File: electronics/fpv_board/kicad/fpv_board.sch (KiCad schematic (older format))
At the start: 12 parts, among them K1 CONN_3, K2 CONN_3, K3 CONN_3, P1 CONN_2, P2 CONN_2, P3 CONN_1, SW1 SWITCH_INV, SW2 SWITCH_INV, SW3 4-SW_DIP, U1 LD1117DT33, U2 L78M05, U3 TX-5800-200

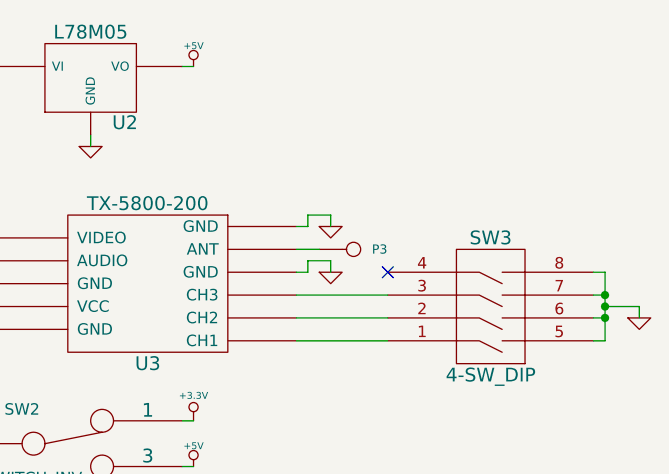
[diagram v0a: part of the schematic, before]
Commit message: Updated FPV board schematic. Started implementation of FPV board PCB. Added .gitignore
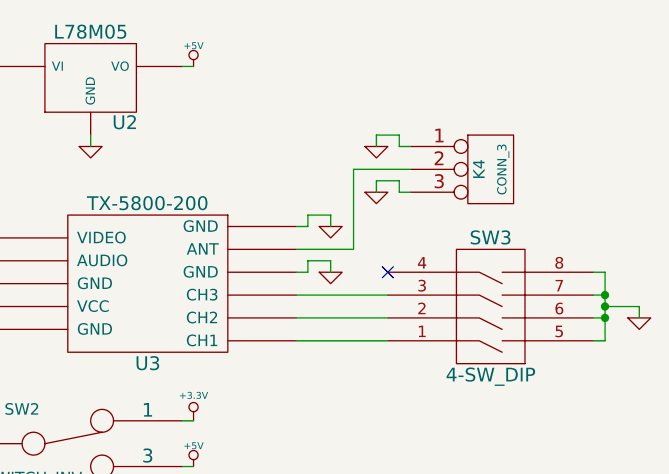
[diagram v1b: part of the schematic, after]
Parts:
- removed P3: CONN_1, symbol CONN_1
- added K4: CONN_3, symbol CONN_3
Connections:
- net GND: now also K4.1 (P1), K4.3 (P3)
- net at U3.10 (ANT): now also K4.2 (PM)
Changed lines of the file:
@@
 NoConn ~ 5350 2000
-$Comp
-L CONN_1 P3
-U 1 1 5381A5F5
-P 5200 1900
-F 0 "P3" H 5280 1900 40  0000 L CNN
-F 1 "CONN_1" H 5200 1955 30  0001 C CNN
-F 2 "" H 5200 1900 60  0000 C CNN
-F 3 "" H 5200 1900 60  0000 C CNN
-	1    5200 1900
-	1    0    0    -1
-$EndComp
-Wire Wire Line
-	4950 1900 5050 1900
 $Comp
 L SWITCH_INV SW1
@@
 	1    0    0    -1
 $EndComp
+$Comp
+L CONN_3 K4
+U 1 1 53826CEB
+P 5800 1550
+F 0 "K4" V 5750 1550 50  0000 C CNN
+F 1 "CONN_3" V 5850 1550 40  0000 C CNN
+F 2 "" H 5800 1550 60  0000 C CNN
+F 3 "" H 5800 1550 60  0000 C CNN
+	1    5800 1550
+	1    0    0    -1
+$EndComp
+$Comp
+L GND #PWR021
+U 1 1 53826CFA
+P 5300 1650
+F 0 "#PWR021" H 5300 1650 30  0001 C CNN
+F 1 "GND" H 5300 1580 30  0001 C CNN
+F 2 "" H 5300 1650 60  0000 C CNN
+F 3 "" H 5300 1650 60  0000 C CNN
+	1    5300 1650
+	1    0    0    -1
+$EndComp
+$Comp
+L GND #PWR022
+U 1 1 53826D09
+P 5300 1450
+F 0 "#PWR022" H 5300 1450 30  0001 C CNN
+F 1 "GND" H 5300 1380 30  0001 C CNN
+F 2 "" H 5300 1450 60  0000 C CNN
+F 3 "" H 5300 1450 60  0000 C CNN
+	1    5300 1450
+	1    0    0    -1
+$EndComp
+Wire Wire Line
+	5450 1450 5400 1450
+Wire Wire Line
+	5400 1450 5400 1400
+Wire Wire Line
+	5400 1400 5300 1400
+Wire Wire Line
+	5300 1400 5300 1450
+Wire Wire Line
+	5450 1650 5400 1650
+Wire Wire Line
+	5400 1650 5400 1600
+Wire Wire Line
+	5400 1600 5300 1600
+Wire Wire Line
+	5300 1600 5300 1650
+Wire Wire Line
+	5450 1550 5200 1550
+Wire Wire Line
+	5200 1550 5200 1900
+Wire Wire Line
+	5200 1900 4950 1900
 $EndSCHEMATC

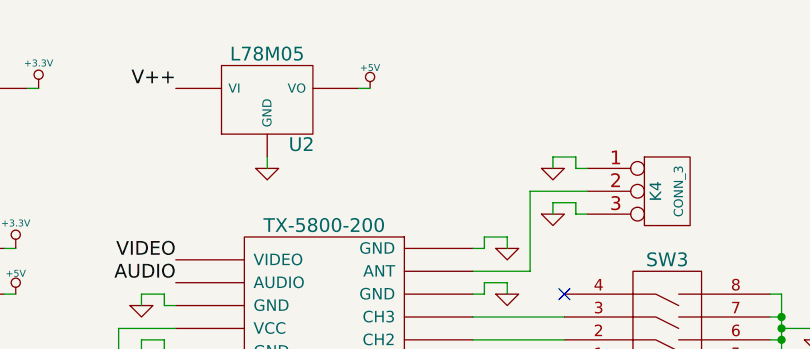
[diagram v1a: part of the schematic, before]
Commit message: Added 5V source selecter jumper to FPV board schematic. Implemented FPV PCB.
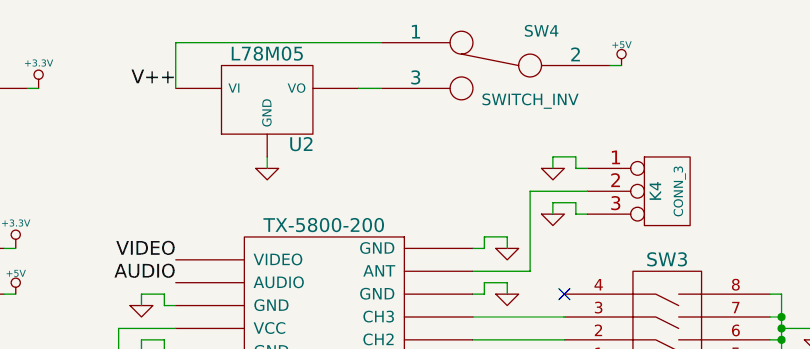
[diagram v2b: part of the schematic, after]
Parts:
- added SW4: SWITCH_INV, ~, symbol SWITCH_INV
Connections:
- net +5V: now also SW4.2; no longer U2.VO
- net V++: now also SW4.1
- new net: SW4.3, U2.VO
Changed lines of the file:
@@
 Sheet 1 1
 Title ""
-Date "25 may 2014"
+Date "27 may 2014"
 Rev ""
 Comp ""
@@
 V++
 $Comp
-L GND #PWR01
+L GND #PWR1
 U 1 1 53815D82
 P 1650 1400
-F 0 "#PWR01" H 1650 1400 30  0001 C CNN
+F 0 "#PWR1" H 1650 1400 30  0001 C CNN
 F 1 "GND" H 1650 1330 30  0001 C CNN
 F 2 "" H 1650 1400 60  0000 C CNN
@@
 $EndComp
 $Comp
-L GND #PWR02
+L GND #PWR2
 U 1 1 53816497
 P 1700 1800
-F 0 "#PWR02" H 1700 1800 30  0001 C CNN
+F 0 "#PWR2" H 1700 1800 30  0001 C CNN
 F 1 "GND" H 1700 1730 30  0001 C CNN
 F 2 "" H 1700 1800 60  0000 C CNN
@@
 $EndComp
 $Comp
-L GND #PWR03
+L GND #PWR4
 U 1 1 538183A2
 P 1700 2850
-F 0 "#PWR03" H 1700 2850 30  0001 C CNN
+F 0 "#PWR4" H 1700 2850 30  0001 C CNN
 F 1 "GND" H 1700 2780 30  0001 C CNN
 F 2 "" H 1700 2850 60  0000 C CNN
@@
 $EndComp
 $Comp
-L GND #PWR04
+L GND #PWR8
 U 1 1 538183B6
 P 2900 2850
-F 0 "#PWR04" H 2900 2850 30  0001 C CNN
+F 0 "#PWR8" H 2900 2850 30  0001 C CNN
 F 1 "GND" H 2900 2780 30  0001 C CNN
 F 2 "" H 2900 2850 60  0000 C CNN
@@
 	2900 2800 2900 2850
 $Comp
-L +5V #PWR05
+L +5V #PWR7
 U 1 1 538183E4
 P 2800 2700
-F 0 "#PWR05" H 2800 2790 20  0001 C CNN
+F 0 "#PWR7" H 2800 2790 20  0001 C CNN
 F 1 "+5V" H 2800 2790 30  0000 C CNN
 F 2 "" H 2800 2700 60  0000 C CNN
@@
 $EndComp
 $Comp
-L +5V #PWR06
+L +5V #PWR10
 U 1 1 538183F3
 P 2950 2000
-F 0 "#PWR06" H 2950 2090 20  0001 C CNN
+F 0 "#PWR10" H 2950 2090 20  0001 C CNN
 F 1 "+5V" H 2950 2090 30  0000 C CNN
 F 2 "" H 2950 2000 60  0000 C CNN
@@
 $EndComp
 $Comp
-L +3.3V #PWR07
+L +3.3V #PWR9
 U 1 1 53818406
 P 2950 1800
-F 0 "#PWR07" H 2950 1760 30  0001 C CNN
+F 0 "#PWR9" H 2950 1760 30  0001 C CNN
 F 1 "+3.3V" H 2950 1910 30  0000 C CNN
 F 2 "" H 2950 1800 60  0000 C CNN
@@
 $EndComp
 $Comp
-L +3.3V #PWR08
+L +3.3V #PWR6
 U 1 1 53818415
 P 2800 2600
-F 0 "#PWR08" H 2800 2560 30  0001 C CNN
+F 0 "#PWR6" H 2800 2560 30  0001 C CNN
 F 1 "+3.3V" H 2800 2710 30  0000 C CNN
 F 2 "" H 2800 2600 60  0000 C CNN
@@
 	2750 2600 2800 2600
 $Comp
-L GND #PWR09
+L GND #PWR3
 U 1 1 538184EF
 P 1700 2500
-F 0 "#PWR09" H 1700 2500 30  0001 C CNN
+F 0 "#PWR3" H 1700 2500 30  0001 C CNN
 F 1 "GND" H 1700 2430 30  0001 C CNN
 F 2 "" H 1700 2500 60  0000 C CNN
@@
 V++
 $Comp
-L +3.3V #PWR010
+L +3.3V #PWR11
 U 1 1 53818937
 P 3050 1100
-F 0 "#PWR010" H 3050 1060 30  0001 C CNN
+F 0 "#PWR11" H 3050 1060 30  0001 C CNN
 F 1 "+3.3V" H 3050 1210 30  0000 C CNN
 F 2 "" H 3050 1100 60  0000 C CNN
@@
 $EndComp
 $Comp
-L +5V #PWR011
+L +5V #PWR21
 U 1 1 53818946
-P 4500 1100
-F 0 "#PWR011" H 4500 1190 20  0001 C CNN
-F 1 "+5V" H 4500 1190 30  0000 C CNN
-F 2 "" H 4500 1100 60  0000 C CNN
-F 3 "" H 4500 1100 60  0000 C CNN
-	1    4500 1100
-	1    0    0    -1
-$EndComp
-$Comp
-L GND #PWR012
+P 5600 1000
+F 0 "#PWR21" H 5600 1090 20  0001 C CNN
+F 1 "+5V" H 5600 1090 30  0000 C CNN
+F 2 "" H 5600 1000 60  0000 C CNN
+F 3 "" H 5600 1000 60  0000 C CNN
+	1    5600 1000
+	1    0    0    -1
+$EndComp
+$Comp
+L GND #PWR5
 U 1 1 53818955
 P 2600 1450
-F 0 "#PWR012" H 2600 1450 30  0001 C CNN
+F 0 "#PWR5" H 2600 1450 30  0001 C CNN
 F 1 "GND" H 2600 1380 30  0001 C CNN
 F 2 "" H 2600 1450 60  0000 C CNN
@@
 $EndComp
 $Comp
-L GND #PWR013
+L GND #PWR14
 U 1 1 53818964
 P 4050 1450
-F 0 "#PWR013" H 4050 1450 30  0001 C CNN
+F 0 "#PWR14" H 4050 1450 30  0001 C CNN
 F 1 "GND" H 4050 1380 30  0001 C CNN
 F 2 "" H 4050 1450 60  0000 C CNN
@@
 Wire Wire Line
 	4050 1400 4050 1450
-Wire Wire Line
-	4450 1100 4500 1100
 $Comp
 L TX-5800-200 U3
@@
 $EndComp
 $Comp
-L GND #PWR014
+L GND #PWR18
 U 1 1 5381A21F
 P 5100 2000
-F 0 "#PWR014" H 5100 2000 30  0001 C CNN
+F 0 "#PWR18" H 5100 2000 30  0001 C CNN
 F 1 "GND" H 5100 1930 30  0001 C CNN
 F 2 "" H 5100 2000 60  0000 C CNN
@@
 $EndComp
 $Comp
-L GND #PWR015
+L GND #PWR17
 U 1 1 5381A22E
 P 5100 1800
-F 0 "#PWR015" H 5100 1800 30  0001 C CNN
+F 0 "#PWR17" H 5100 1800 30  0001 C CNN
 F 1 "GND" H 5100 1730 30  0001 C CNN
 F 2 "" H 5100 1800 60  0000 C CNN
@@
 $EndComp
 $Comp
-L GND #PWR016
+L GND #PWR12
 U 1 1 5381A23D
 P 3500 2050
-F 0 "#PWR016" H 3500 2050 30  0001 C CNN
+F 0 "#PWR12" H 3500 2050 30  0001 C CNN
 F 1 "GND" H 3500 1980 30  0001 C CNN
 F 2 "" H 3500 2050 60  0000 C CNN
@@
 $EndComp
 $Comp
-L GND #PWR017
+L GND #PWR13
 U 1 1 5381A24C
 P 3500 2250
-F 0 "#PWR017" H 3500 2250 30  0001 C CNN
+F 0 "#PWR13" H 3500 2250 30  0001 C CNN
 F 1 "GND" H 3500 2180 30  0001 C CNN
 F 2 "" H 3500 2250 60  0000 C CNN
@@
 	4950 2100 5350 2100
 $Comp
-L GND #PWR018
+L GND #PWR22
 U 1 1 5381A3E8
 P 6450 2200
-F 0 "#PWR018" H 6450 2200 30  0001 C CNN
+F 0 "#PWR22" H 6450 2200 30  0001 C CNN
 F 1 "GND" H 6450 2130 30  0001 C CNN
 F 2 "" H 6450 2200 60  0000 C CNN
@@
 	4450 2850 4500 2850
 $Comp
-L +3.3V #PWR019
+L +3.3V #PWR15
 U 1 1 5381A8C7
 P 4500 2650
-F 0 "#PWR019" H 4500 2610 30  0001 C CNN
+F 0 "#PWR15" H 4500 2610 30  0001 C CNN
 F 1 "+3.3V" H 4500 2760 30  0000 C CNN
 F 2 "" H 4500 2650 60  0000 C CNN
@@
 $EndComp
 $Comp
-L +5V #PWR020
+L +5V #PWR16
 U 1 1 5381A8D6
 P 4500 2850
-F 0 "#PWR020" H 4500 2940 20  0001 C CNN
+F 0 "#PWR16" H 4500 2940 20  0001 C CNN
 F 1 "+5V" H 4500 2940 30  0000 C CNN
 F 2 "" H 4500 2850 60  0000 C CNN
@@
 $EndComp
 $Comp
-L GND #PWR021
+L GND #PWR20
 U 1 1 53826CFA
 P 5300 1650
-F 0 "#PWR021" H 5300 1650 30  0001 C CNN
+F 0 "#PWR20" H 5300 1650 30  0001 C CNN
 F 1 "GND" H 5300 1580 30  0001 C CNN
 F 2 "" H 5300 1650 60  0000 C CNN
@@
 $EndComp
 $Comp
-L GND #PWR022
+L GND #PWR19
 U 1 1 53826D09
 P 5300 1450
-F 0 "#PWR022" H 5300 1450 30  0001 C CNN
+F 0 "#PWR19" H 5300 1450 30  0001 C CNN
 F 1 "GND" H 5300 1380 30  0001 C CNN
 F 2 "" H 5300 1450 60  0000 C CNN
@@
 Wire Wire Line
 	5200 1900 4950 1900
+$Comp
+L SWITCH_INV SW4
+U 1 1 53851F8C
+P 5050 1000
+F 0 "SW4" H 4850 1150 50  0000 C CNN
+F 1 "SWITCH_INV" H 4900 850 50  0000 C CNN
+F 2 "~" H 5050 1000 60  0000 C CNN
+F 3 "~" H 5050 1000 60  0000 C CNN
+	1    5050 1000
+	-1   0    0    -1
+$EndComp
+Wire Wire Line
+	5550 1000 5600 1000
+Wire Wire Line
+	4450 1100 4550 1100
+Wire Wire Line
+	4550 900  3650 900
+Wire Wire Line
+	3650 900  3650 1100
 $EndSCHEMATC
